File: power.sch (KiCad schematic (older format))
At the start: 10 parts, among them P6 CONN_01X02, U9 LD2981

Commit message: Added missing foorprint for C3
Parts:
- C3: footprint (none) -> Capacitors_ThroughHole:C_Radial_D6.3_L11.2_P2.5
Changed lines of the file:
@@
 F 0 "C3" H 2075 3350 50  0000 L CNN
 F 1 "100u" H 2075 3150 50  0000 L CNN
-F 2 "" H 2050 3250 50  0000 C CNN
+F 2 "Capacitors_ThroughHole:C_Radial_D6.3_L11.2_P2.5" H 2050 3250 50  0001 C CNN
 F 3 "" H 2050 3250 50  0000 C CNN
 	1    2050 3250

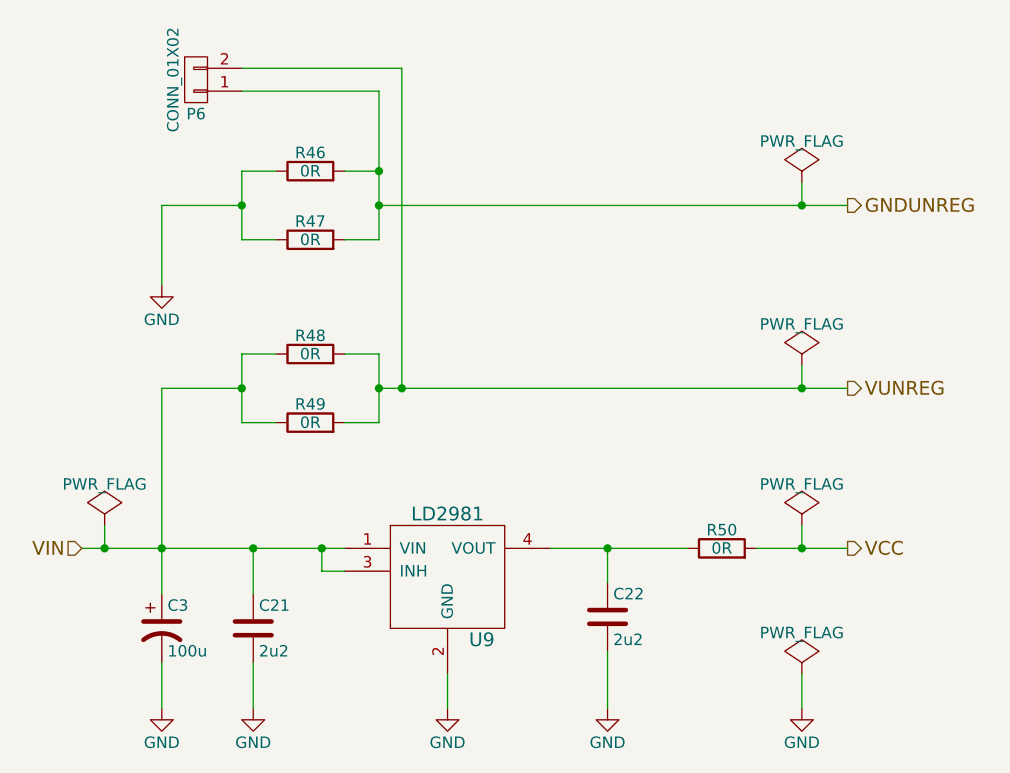
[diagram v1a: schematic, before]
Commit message: Removed 0R resistors and started new layout
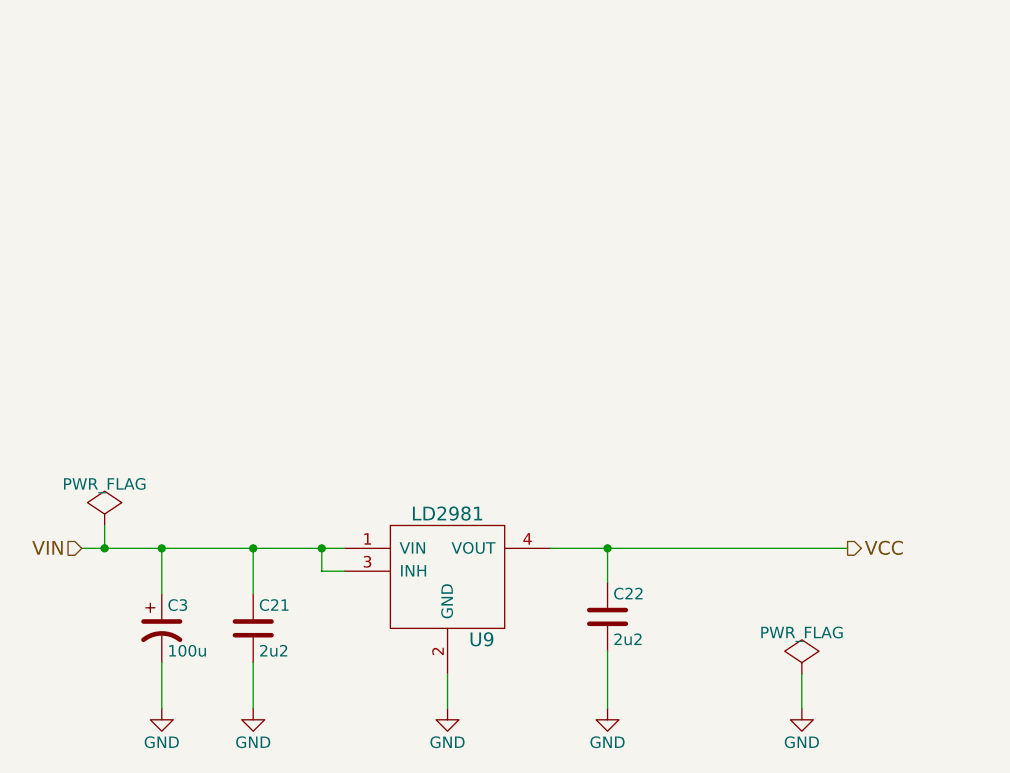
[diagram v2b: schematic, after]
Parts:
- removed P6: CONN_01X02, Pin_Headers:Pin_Header_Straight_1x02, symbol CONN_01X02
- removed R46, R47, R48, R49, R50: 0R, olof:R_0805_HandSoldering, symbol R
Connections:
- net VCC: now also C22.1, U9.4 (VOUT)
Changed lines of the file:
@@
 	1    0    0    -1
 $EndComp
-Wire Wire Line
-	2050 2200 2050 3100
 $Comp
-L GND #PWR067
+L GND #PWR077
 U 1 1 5B1DDF36
 P 2050 3600
-F 0 "#PWR067" H 2050 3350 50  0001 C CNN
+F 0 "#PWR077" H 2050 3350 50  0001 C CNN
 F 1 "GND" H 2050 3450 50  0000 C CNN
 F 2 "" H 2050 3600 50  0000 C CNN
@@
 Connection ~ 2750 2900
 $Comp
-L GND #PWR068
+L GND #PWR078
 U 1 1 5B1E34D5
 P 3300 3600
-F 0 "#PWR068" H 3300 3350 50  0001 C CNN
+F 0 "#PWR078" H 3300 3350 50  0001 C CNN
 F 1 "GND" H 3300 3450 50  0000 C CNN
 F 2 "" H 3300 3600 50  0000 C CNN
@@
 	3300 3450 3300 3600
 Wire Wire Line
-	3750 2900 4350 2900
+	3750 2900 5050 2900
 Wire Wire Line
 	1700 2900 2850 2900
@@
 Connection ~ 2450 2900
 $Comp
-L GND #PWR069
+L GND #PWR079
 U 1 1 5B1E3594
 P 2450 3600
-F 0 "#PWR069" H 2450 3350 50  0001 C CNN
+F 0 "#PWR079" H 2450 3350 50  0001 C CNN
 F 1 "GND" H 2450 3450 50  0000 C CNN
 F 2 "" H 2450 3600 50  0000 C CNN
@@
 Connection ~ 4000 2900
 $Comp
-L GND #PWR070
+L GND #PWR080
 U 1 1 5B1E36FB
 P 4000 3600
-F 0 "#PWR070" H 4000 3350 50  0001 C CNN
+F 0 "#PWR080" H 4000 3350 50  0001 C CNN
 F 1 "GND" H 4000 3450 50  0000 C CNN
 F 2 "" H 4000 3600 50  0000 C CNN
@@
 Wire Wire Line
 	4000 3600 4000 3350
-Text HLabel 5050 2200 2    60   Output ~ 0
-VUNREG
-Wire Wire Line
-	3000 2200 5050 2200
-$Comp
-L R R48
-U 1 1 5B1E447E
-P 2700 2050
-F 0 "R48" V 2780 2050 50  0000 C CNN
-F 1 "0R" V 2700 2050 50  0000 C CNN
-F 2 "olof:R_0805_HandSoldering" V 2630 2050 50  0001 C CNN
-F 3 "" H 2700 2050 50  0000 C CNN
-	1    2700 2050
-	0    -1   -1   0
-$EndComp
-$Comp
-L R R49
-U 1 1 5B1E47A7
-P 2700 2350
-F 0 "R49" V 2780 2350 50  0000 C CNN
-F 1 "0R" V 2700 2350 50  0000 C CNN
-F 2 "olof:R_0805_HandSoldering" V 2630 2350 50  0001 C CNN
-F 3 "" H 2700 2350 50  0000 C CNN
-	1    2700 2350
-	0    -1   -1   0
-$EndComp
-Wire Wire Line
-	2850 2050 3000 2050
-Wire Wire Line
-	3000 2050 3000 2350
-Wire Wire Line
-	3000 2350 2850 2350
-Connection ~ 3000 2200
-Wire Wire Line
-	2550 2050 2400 2050
-Wire Wire Line
-	2400 2050 2400 2350
-Wire Wire Line
-	2400 2350 2550 2350
-Wire Wire Line
-	2400 2200 2050 2200
-Connection ~ 2400 2200
-Text HLabel 5050 1400 2    60   Output ~ 0
-GNDUNREG
-$Comp
-L R R46
-U 1 1 5B1E4940
-P 2700 1250
-F 0 "R46" V 2780 1250 50  0000 C CNN
-F 1 "0R" V 2700 1250 50  0000 C CNN
-F 2 "olof:R_0805_HandSoldering" V 2630 1250 50  0001 C CNN
-F 3 "" H 2700 1250 50  0000 C CNN
-	1    2700 1250
-	0    -1   -1   0
-$EndComp
-$Comp
-L R R47
-U 1 1 5B1E4A49
-P 2700 1550
-F 0 "R47" V 2780 1550 50  0000 C CNN
-F 1 "0R" V 2700 1550 50  0000 C CNN
-F 2 "olof:R_0805_HandSoldering" V 2630 1550 50  0001 C CNN
-F 3 "" H 2700 1550 50  0000 C CNN
-	1    2700 1550
-	0    -1   -1   0
-$EndComp
-Wire Wire Line
-	2850 1250 3000 1250
-Wire Wire Line
-	3000 900  3000 1550
-Wire Wire Line
-	3000 1550 2850 1550
-Wire Wire Line
-	2550 1250 2400 1250
-Wire Wire Line
-	2400 1250 2400 1550
-Wire Wire Line
-	2400 1550 2550 1550
-Wire Wire Line
-	2400 1400 2050 1400
-Wire Wire Line
-	2050 1400 2050 1750
-Connection ~ 2400 1400
-$Comp
-L GND #PWR071
-U 1 1 5B1E4B00
-P 2050 1750
-F 0 "#PWR071" H 2050 1500 50  0001 C CNN
-F 1 "GND" H 2050 1600 50  0000 C CNN
-F 2 "" H 2050 1750 50  0000 C CNN
-F 3 "" H 2050 1750 50  0000 C CNN
-	1    2050 1750
-	1    0    0    -1
-$EndComp
-Wire Wire Line
-	3000 1400 5050 1400
-Connection ~ 3000 1400
-$Comp
-L CONN_01X02 P6
-U 1 1 5B1E4F7B
-P 2200 850
-F 0 "P6" H 2200 1000 50  0000 C CNN
-F 1 "CONN_01X02" V 2300 850 50  0000 C CNN
-F 2 "Pin_Headers:Pin_Header_Straight_1x02" H 2200 850 50  0001 C CNN
-F 3 "" H 2200 850 50  0000 C CNN
-	1    2200 850
-	-1   0    0    1
-$EndComp
-Wire Wire Line
-	2400 900  3000 900
-Connection ~ 3000 1250
-Wire Wire Line
-	2400 800  3100 800
-Wire Wire Line
-	3100 800  3100 2200
-Connection ~ 3100 2200
-$Comp
-L PWR_FLAG #FLG072
-U 1 1 5B1E5277
-P 4850 1300
-F 0 "#FLG072" H 4850 1395 50  0001 C CNN
-F 1 "PWR_FLAG" H 4850 1480 50  0000 C CNN
-F 2 "" H 4850 1300 50  0000 C CNN
-F 3 "" H 4850 1300 50  0000 C CNN
-	1    4850 1300
-	1    0    0    -1
-$EndComp
-$Comp
-L PWR_FLAG #FLG073
-U 1 1 5B1E52A4
-P 4850 2100
-F 0 "#FLG073" H 4850 2195 50  0001 C CNN
-F 1 "PWR_FLAG" H 4850 2280 50  0000 C CNN
-F 2 "" H 4850 2100 50  0000 C CNN
-F 3 "" H 4850 2100 50  0000 C CNN
-	1    4850 2100
-	1    0    0    -1
-$EndComp
-Wire Wire Line
-	4850 2100 4850 2200
-Connection ~ 4850 2200
-Wire Wire Line
-	4850 1300 4850 1400
-Connection ~ 4850 1400
-$Comp
-L R R50
-U 1 1 5B1F106C
-P 4500 2900
-F 0 "R50" V 4580 2900 50  0000 C CNN
-F 1 "0R" V 4500 2900 50  0000 C CNN
-F 2 "olof:R_0805_HandSoldering" V 4430 2900 50  0001 C CNN
-F 3 "" H 4500 2900 50  0000 C CNN
-	1    4500 2900
-	0    -1   -1   0
-$EndComp
-Wire Wire Line
-	5050 2900 4650 2900
 $Comp
 L C C22
@@
 $EndComp
 $Comp
-L PWR_FLAG #FLG074
-U 1 1 5B1F7644
-P 4850 2800
-F 0 "#FLG074" H 4850 2895 50  0001 C CNN
-F 1 "PWR_FLAG" H 4850 2980 50  0000 C CNN
-F 2 "" H 4850 2800 50  0000 C CNN
-F 3 "" H 4850 2800 50  0000 C CNN
-	1    4850 2800
-	1    0    0    -1
-$EndComp
-Wire Wire Line
-	4850 2800 4850 2900
-Connection ~ 4850 2900
-$Comp
-L PWR_FLAG #FLG075
+L PWR_FLAG #FLG081
 U 1 1 5B1F80D6
 P 4850 3450
-F 0 "#FLG075" H 4850 3545 50  0001 C CNN
+F 0 "#FLG081" H 4850 3545 50  0001 C CNN
 F 1 "PWR_FLAG" H 4850 3630 50  0000 C CNN
 F 2 "" H 4850 3450 50  0000 C CNN
@@
 $EndComp
 $Comp
-L GND #PWR076
+L GND #PWR082
 U 1 1 5B1F80FF
 P 4850 3600
-F 0 "#PWR076" H 4850 3350 50  0001 C CNN
+F 0 "#PWR082" H 4850 3350 50  0001 C CNN
 F 1 "GND" H 4850 3450 50  0000 C CNN
 F 2 "" H 4850 3600 50  0000 C CNN
@@
 	4850 3450 4850 3600
 $Comp
-L PWR_FLAG #FLG077
+L PWR_FLAG #FLG083
 U 1 1 5B1F8317
 P 1800 2800
-F 0 "#FLG077" H 1800 2895 50  0001 C CNN
+F 0 "#FLG083" H 1800 2895 50  0001 C CNN
 F 1 "PWR_FLAG" H 1800 2980 50  0000 C CNN
 F 2 "" H 1800 2800 50  0000 C CNN
@@
 	1800 2800 1800 2900
 Connection ~ 1800 2900
+Wire Wire Line
+	2050 2900 2050 3100
 $EndSCHEMATC
